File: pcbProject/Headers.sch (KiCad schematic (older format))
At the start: 4 parts, among them P1 Power Header, P2 Analog Header (AD), P3 Digital Header 02 (IOH), P4 Digital Header 01 (IOL)

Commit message: schema Afgewerkt
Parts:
- removed P2: Analog Header (AD), ~, symbol Arduino_Uno_R3_From_Scratch-rescue:CONN_01X06
- added P2: P2 Analog Header (AD), symbol Arduino_Uno_R3_From_Scratch-rescue:CONN_01X08
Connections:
- net ARD_AN0: now also P2.1 (P1)
- net ARD_AN1: now also P2.2 (P2)
- net ARD_AN2: now also P2.3 (P3)
- net ARD_AN3: now also P2.4 (P4)
- net ARD_AN4/SDA: now also P2.5 (P5)
- net ARD_AN5/SCL: now also P2.6 (P6)
- new net ARD_AN6: P2.7 (P7)
- new net ARD_AN7: P2.8 (P8)
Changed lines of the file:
@@
 $EndDescr
-$Comp
-L Arduino_Uno_R3_From_Scratch-rescue:CONN_01X06 P2
-U 1 1 55E94764
-P 6250 3325
-F 0 "P2" H 6400 3200 60  0000 L CNN
-F 1 "Analog Header (AD)" H 6400 3325 60  0000 L CNN
-F 2 "~" H 6250 3325 60  0000 C CNN
-F 3 "http://sullinscorp.com/catalogs/101_PAGE114-115_.100_FEMALE_HDR.pdf" H 6250 3325 60  0001 C CNN
-F 4 "Connector Header 6 Position 0.100\" (2.54mm) Gold Surface Mount" H 6250 3325 60  0001 C CNN "Characteristics"
-F 5 "Shield Header 6POS - ANLG" H 6250 3325 60  0001 C CNN "Description"
-F 6 "Sullins Connector" H 6250 3325 60  0001 C CNN "MFN"
-F 7 "NPPC061KFXC-RC" H 6250 3325 60  0001 C CNN "MFP"
-F 8 "SMD" H 6250 3325 60  0001 C CNN "Package ID"
-F 9 "ANY" H 6250 3325 60  0001 C CNN "Source"
-F 10 "N" H 6250 3325 60  0001 C CNN "Critical"
-F 11 "Shield_Headers" H 6250 3325 60  0001 C CNN "Subsystem"
-F 12 "~" H 6250 3325 60  0001 C CNN "Notes"
-	1    6250 3325
-	1    0    0    1
-$EndComp
 $Comp
 L Arduino_Uno_R3_From_Scratch:5V_LDO #PWR035
@@
 Text HLabel 4800 2725 0    40   Input ~ 0
 328P_RESET
-Text HLabel 4775 3275 0    40   Input ~ 0
+Text HLabel 4800 3475 0    40   Input ~ 0
 ARD_AN3
-Text HLabel 4775 3375 0    40   Input ~ 0
+Text HLabel 4800 3575 0    40   Input ~ 0
 ARD_AN2
-Text HLabel 4775 3475 0    40   Input ~ 0
+Text HLabel 4800 3675 0    40   Input ~ 0
 ARD_AN1
-Text HLabel 4775 3575 0    40   Input ~ 0
+Text HLabel 4800 3775 0    40   Input ~ 0
 ARD_AN0
-Wire Wire Line
-	4775 3575 6050 3575
-Wire Wire Line
-	6050 3475 4775 3475
-Wire Wire Line
-	4775 3375 6050 3375
-Wire Wire Line
-	6050 3275 4775 3275
 Text HLabel 4775 5175 0    40   Input ~ 0
 ARD_DIG7
@@
 	1    0    0    -1
 $EndComp
-Text HLabel 4800 3175 0    40   Input ~ 0
+Text HLabel 4825 3375 0    40   Input ~ 0
 ARD_AN4/SDA
-Text HLabel 4800 3075 0    40   Input ~ 0
+Text HLabel 4825 3275 0    40   Input ~ 0
 ARD_AN5/SCL
-Wire Wire Line
-	4800 3075 6050 3075
-Wire Wire Line
-	4800 3175 6050 3175
 Text HLabel 4750 4800 0    40   Input ~ 0
 ARD_DIG8
@@
 Wire Wire Line
 	6050 4700 4750 4700
+$Comp
+L Arduino_Uno_R3_From_Scratch-rescue:CONN_01X08 P2
+U 1 1 5C79CCDA
+P 6250 3425
+F 0 "P2" H 6168 2850 50  0000 C CNN
+F 1 "P2 Analog Header (AD)" H 6825 3400 50  0000 C CNN
+F 2 "" H 6250 3425 60  0000 C CNN
+F 3 "" H 6250 3425 60  0000 C CNN
+	1    6250 3425
+	1    0    0    1
+$EndComp
+Wire Wire Line
+	4800 3775 6050 3775
+Wire Wire Line
+	4800 3675 6050 3675
+Wire Wire Line
+	4800 3575 6050 3575
+Wire Wire Line
+	4800 3475 6050 3475
+Wire Wire Line
+	4825 3375 6050 3375
+Wire Wire Line
+	4825 3275 6050 3275
+Text HLabel 4825 3175 0    50   Input ~ 0
+ARD_AN6
+Text HLabel 4825 3075 0    50   Input ~ 0
+ARD_AN7
+Wire Wire Line
+	4825 3175 6050 3175
+Wire Wire Line
+	4825 3075 6050 3075
 $EndSCHEMATC

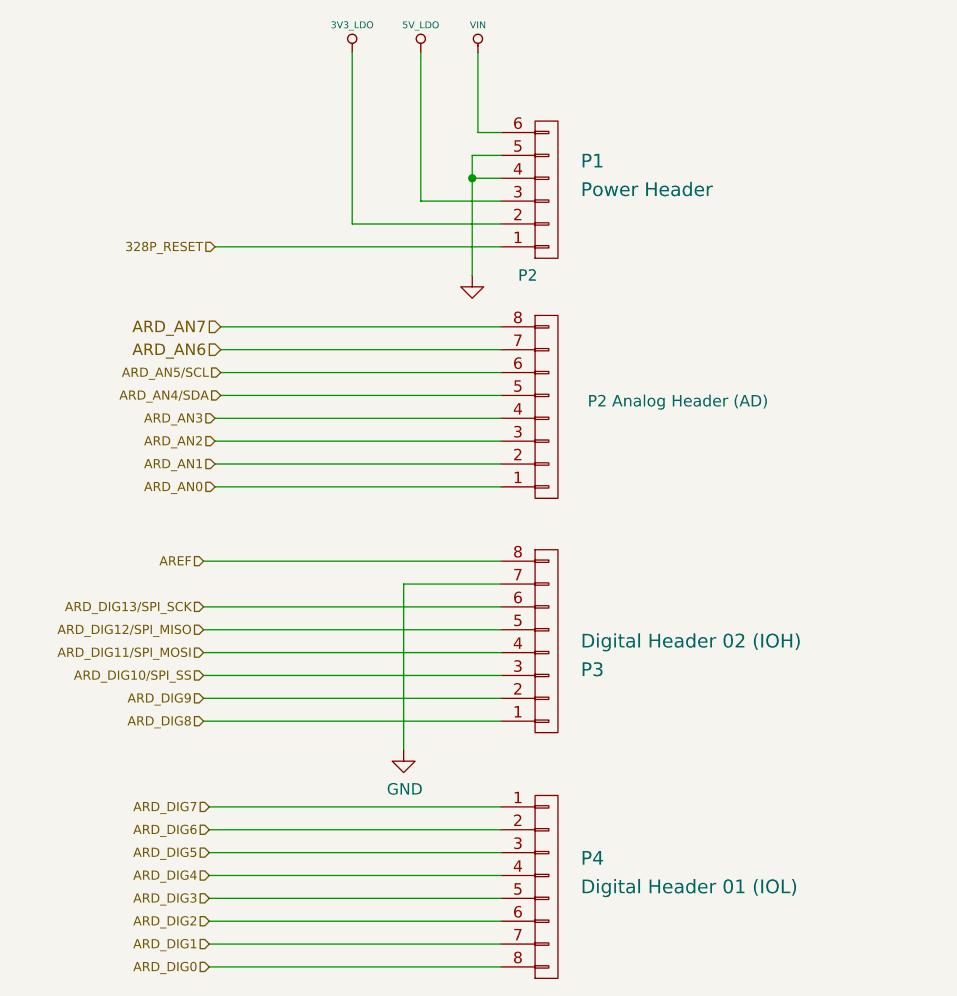
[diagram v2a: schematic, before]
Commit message: TekeningAfenGecontroleerd
nu nog componenten toevoegen en routen
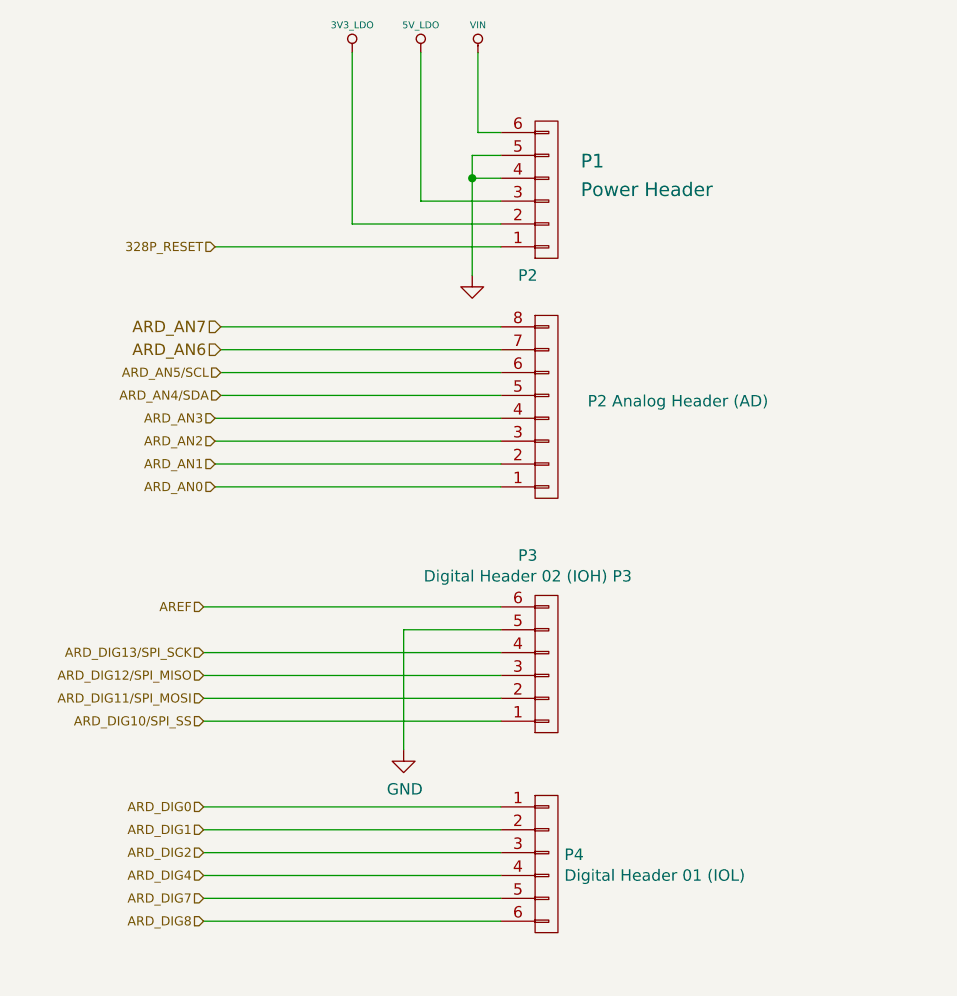
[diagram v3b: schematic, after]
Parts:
- removed P3: Digital Header 02 (IOH), ~, symbol Arduino_Uno_R3_From_Scratch-rescue:CONN_01X08
- removed P4: Digital Header 01 (IOL), ~, symbol Arduino_Uno_R3_From_Scratch-rescue:CONN_01X08
- added P3: Digital Header 02 (IOH) P3, symbol Arduino_Uno_R3_From_Scratch-rescue:CONN_01X06
- added P4: Digital Header 01 (IOL), symbol Arduino_Uno_R3_From_Scratch-rescue:CONN_01X06
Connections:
- net ARD_DIG0: now also P4.1 (P1)
- net ARD_DIG1: now also P4.2 (P2)
- net ARD_DIG10/SPI_SS: now also P3.1 (P1)
- net ARD_DIG11/SPI_MOSI: now also P3.2 (P2)
- net ARD_DIG12/SPI_MISO: now also P3.3 (P3)
- net ARD_DIG13/SPI_SCK: now also P3.4 (P4)
- net ARD_DIG2: now also P4.3 (P3)
- net ARD_DIG4: now also P4.4 (P4)
- net ARD_DIG7: now also P4.5 (P5)
- net ARD_DIG8: now also P4.6 (P6)
- net AREF: now also P3.6 (P6)
- net GND: now also P3.5 (P5)
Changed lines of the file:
@@
 Text HLabel 4800 3775 0    40   Input ~ 0
 ARD_AN0
-Text HLabel 4775 5175 0    40   Input ~ 0
+Text HLabel 4750 5575 0    40   Input ~ 0
 ARD_DIG7
-Text HLabel 4775 5275 0    40   Input ~ 0
-ARD_DIG6
-Text HLabel 4775 5375 0    40   Input ~ 0
-ARD_DIG5
-Text HLabel 4775 5475 0    40   Input ~ 0
+Text HLabel 4750 5475 0    40   Input ~ 0
 ARD_DIG4
-Text HLabel 4775 5575 0    40   Input ~ 0
-ARD_DIG3
-Text HLabel 4775 5675 0    40   Input ~ 0
+Text HLabel 4750 5375 0    40   Input ~ 0
 ARD_DIG2
-Text HLabel 4775 5775 0    40   Input ~ 0
+Text HLabel 4750 5275 0    40   Input ~ 0
 ARD_DIG1
-Text HLabel 4775 5875 0    40   Input ~ 0
+Text HLabel 4750 5175 0    40   Input ~ 0
 ARD_DIG0
-Wire Wire Line
-	6050 5175 4775 5175
-Wire Wire Line
-	4775 5275 6050 5275
-Wire Wire Line
-	6050 5375 4775 5375
-Wire Wire Line
-	4775 5475 6050 5475
-Wire Wire Line
-	6050 5575 4775 5575
-Wire Wire Line
-	4775 5675 6050 5675
-Wire Wire Line
-	6050 5775 4775 5775
-Wire Wire Line
-	4775 5875 6050 5875
-$Comp
-L Arduino_Uno_R3_From_Scratch-rescue:CONN_01X08 P4
-U 1 1 5615BF57
-P 6250 5525
-F 0 "P4" H 6400 5650 60  0000 L CNN
-F 1 "Digital Header 01 (IOL)" H 6400 5525 60  0000 L CNN
-F 2 "~" H 6250 5525 60  0000 C CNN
-F 3 "http://sullinscorp.com/catalogs/101_PAGE114-115_.100_FEMALE_HDR.pdf" H 6250 5525 60  0001 C CNN
-F 4 "Connector Header 8 Position 0.100\" (2.54mm) Gold Surface Mount" H 6250 5525 60  0001 C CNN "Characteristics"
-F 5 "Shield Header 8POS - DIG01" H 6250 5525 60  0001 C CNN "Description"
-F 6 "Sullins Connector" H 6250 5525 60  0001 C CNN "MFN"
-F 7 "NPPC081KFXC-RC" H 6250 5525 60  0001 C CNN "MFP"
-F 8 "SMD" H 6250 5525 60  0001 C CNN "Package ID"
-F 9 "ANY" H 6250 5525 60  0001 C CNN "Source"
-F 10 "N" H 6250 5525 60  0001 C CNN "Critical"
-F 11 "Shield_Headers" H 6250 5525 60  0001 C CNN "Subsystem"
-F 12 "~" H 6250 5525 60  0001 C CNN "Notes"
-	1    6250 5525
-	1    0    0    -1
-$EndComp
 Text HLabel 4825 3375 0    40   Input ~ 0
 ARD_AN4/SDA
 Text HLabel 4825 3275 0    40   Input ~ 0
 ARD_AN5/SCL
+Text HLabel 4750 5675 0    40   Input ~ 0
+ARD_DIG8
 Text HLabel 4750 4800 0    40   Input ~ 0
-ARD_DIG8
+ARD_DIG10/SPI_SS
 Text HLabel 4750 4700 0    40   Input ~ 0
-ARD_DIG9
+ARD_DIG11/SPI_MOSI
 Text HLabel 4750 4600 0    40   Input ~ 0
-ARD_DIG10/SPI_SS
+ARD_DIG12/SPI_MISO
 Text HLabel 4750 4500 0    40   Input ~ 0
-ARD_DIG11/SPI_MOSI
-Text HLabel 4750 4400 0    40   Input ~ 0
-ARD_DIG12/SPI_MISO
+ARD_DIG13/SPI_SCK
 Text HLabel 4750 4300 0    40   Input ~ 0
-ARD_DIG13/SPI_SCK
-Text HLabel 4750 4100 0    40   Input ~ 0
 AREF
 $Comp
@@
 	5950 2225 6050 2225
 $Comp
-L Arduino_Uno_R3_From_Scratch-rescue:CONN_01X08 P3
-U 1 1 5C578D54
-P 6250 4450
-F 0 "P3" H 6400 4575 60  0000 L CNN
-F 1 "Digital Header 02 (IOH)" H 6400 4450 60  0000 L CNN
-F 2 "~" H 6250 4450 60  0000 C CNN
-F 3 "http://sullinscorp.com/catalogs/101_PAGE114-115_.100_FEMALE_HDR.pdf" H 6250 4450 60  0001 C CNN
-F 4 "Connector Header 8 Position 0.100\" (2.54mm) Gold Surface Mount" H 6250 4450 60  0001 C CNN "Characteristics"
-F 5 "Shield Header 8POS - DIG01" H 6250 4450 60  0001 C CNN "Description"
-F 6 "Sullins Connector" H 6250 4450 60  0001 C CNN "MFN"
-F 7 "NPPC081KFXC-RC" H 6250 4450 60  0001 C CNN "MFP"
-F 8 "SMD" H 6250 4450 60  0001 C CNN "Package ID"
-F 9 "ANY" H 6250 4450 60  0001 C CNN "Source"
-F 10 "N" H 6250 4450 60  0001 C CNN "Critical"
-F 11 "Shield_Headers" H 6250 4450 60  0001 C CNN "Subsystem"
-F 12 "~" H 6250 4450 60  0001 C CNN "Notes"
-	1    6250 4450
-	1    0    0    1
-$EndComp
-Wire Wire Line
-	6050 4100 4750 4100
-$Comp
 L power:GND #PWR0101
 U 1 1 5C579B64
@@
 $EndComp
 Wire Wire Line
-	6050 4200 5625 4200
-Wire Wire Line
-	5625 4200 5625 4925
-Wire Wire Line
 	6050 4300 4750 4300
-Wire Wire Line
-	6050 4400 4750 4400
 Wire Wire Line
 	6050 4500 4750 4500
 Wire Wire Line
 	6050 4600 4750 4600
-Wire Wire Line
-	6050 4800 4750 4800
-Wire Wire Line
-	6050 4700 4750 4700
 $Comp
 L Arduino_Uno_R3_From_Scratch-rescue:CONN_01X08 P2
@@
 Wire Wire Line
 	4825 3075 6050 3075
+Wire Wire Line
+	4750 5175 6050 5175
+Wire Wire Line
+	4750 5275 6050 5275
+Wire Wire Line
+	4750 5375 6050 5375
+Wire Wire Line
+	4750 5475 6050 5475
+Wire Wire Line
+	4750 5575 6050 5575
+Wire Wire Line
+	4750 5675 6050 5675
+Wire Wire Line
+	4750 4800 6050 4800
+Wire Wire Line
+	4750 4700 6050 4700
+Wire Wire Line
+	6050 4400 5625 4400
+Wire Wire Line
+	5625 4400 5625 4925
+$Comp
+L Arduino_Uno_R3_From_Scratch-rescue:CONN_01X06 P3
+U 1 1 5C9A72A7
+P 6250 4550
+F 0 "P3" H 6168 4075 50  0000 C CNN
+F 1 "Digital Header 02 (IOH) P3" H 6168 4166 50  0000 C CNN
+F 2 "" H 6250 4550 60  0000 C CNN
+F 3 "" H 6250 4550 60  0000 C CNN
+	1    6250 4550
+	1    0    0    1
+$EndComp
+$Comp
+L Arduino_Uno_R3_From_Scratch-rescue:CONN_01X06 P4
+U 1 1 5C9A74BA
+P 6250 5425
+F 0 "P4" H 6328 5466 50  0000 L CNN
+F 1 "Digital Header 01 (IOL)" H 6328 5375 50  0000 L CNN
+F 2 "" H 6250 5425 60  0000 C CNN
+F 3 "" H 6250 5425 60  0000 C CNN
+	1    6250 5425
+	1    0    0    -1
+$EndComp
 $EndSCHEMATC

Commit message: deel1routingpcb
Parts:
- P1: footprint ~ -> Connector_PinSocket_2.54mm:PinSocket_1x06_P2.54mm_Vertical
- P2: footprint (none) -> Connector_PinSocket_2.54mm:PinSocket_1x08_P2.54mm_Vertical
- P3, P4: footprint (none) -> Connector_PinSocket_2.54mm:PinSocket_1x06_P2.54mm_Vertical
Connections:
- net Vin is gone; now on net 3V3_LDO: P1.6 (P6)
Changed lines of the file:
@@
-	1    0    0    -1
-$EndComp
-$Comp
-L Arduino_Uno_R3_From_Scratch:Vin #PWR037
-U 1 1 55E95DA2
-P 5950 1875
-F 0 "#PWR037" H 5950 1965 20  0001 C CNN
-F 1 "VIN" H 5950 1995 30  0000 C CNN
-F 2 "~" H 5950 1875 60  0000 C CNN
-F 3 "~" H 5950 1875 60  0000 C CNN
-	1    5950 1875
 	1    0    0    -1
 $EndComp
@@
 F 0 "P1" H 6400 2350 60  0000 L CNN
 F 1 "Power Header" H 6400 2475 60  0000 L CNN
-F 2 "~" H 6250 2475 60  0000 C CNN
+F 2 "Connector_PinSocket_2.54mm:PinSocket_1x06_P2.54mm_Vertical" H 6250 2475 60  0000 C CNN
 F 3 "http://sullinscorp.com/catalogs/101_PAGE114-115_.100_FEMALE_HDR.pdf" H 6250 2475 60  0001 C CNN
 F 4 "Connector Header 6 Position 0.100\" (2.54mm) Gold Surface Mount" H 6250 2475 60  0001 C CNN "Characteristics"
@@
 	5400 2625 6050 2625
 Wire Wire Line
-	5400 1875 5400 2625
+	5400 1875 5400 2225
 Wire Wire Line
 	5700 2525 6050 2525
@@
 Wire Wire Line
 	5925 2425 5925 2850
-Wire Wire Line
-	5950 1875 5950 2225
-Wire Wire Line
-	5950 2225 6050 2225
 $Comp
 L power:GND #PWR0101
@@
 F 0 "P2" H 6168 2850 50  0000 C CNN
 F 1 "P2 Analog Header (AD)" H 6825 3400 50  0000 C CNN
-F 2 "" H 6250 3425 60  0001 C CNN
+F 2 "Connector_PinSocket_2.54mm:PinSocket_1x08_P2.54mm_Vertical" H 6250 3425 60  0001 C CNN
 F 3 "" H 6250 3425 60  0000 C CNN
 	1    6250 3425
@@
 F 0 "P3" H 6168 4075 50  0000 C CNN
 F 1 "Digital Header 02 (IOH) P3" H 6168 4166 50  0000 C CNN
-F 2 "" H 6250 4550 60  0000 C CNN
+F 2 "Connector_PinSocket_2.54mm:PinSocket_1x06_P2.54mm_Vertical" H 6250 4550 60  0001 C CNN
 F 3 "" H 6250 4550 60  0000 C CNN
 	1    6250 4550
@@
 F 0 "P4" H 6328 5466 50  0000 L CNN
 F 1 "Digital Header 01 (IOL)" H 6328 5375 50  0000 L CNN
-F 2 "" H 6250 5425 60  0000 C CNN
+F 2 "Connector_PinSocket_2.54mm:PinSocket_1x06_P2.54mm_Vertical" H 6250 5425 60  0001 C CNN
 F 3 "" H 6250 5425 60  0000 C CNN
 	1    6250 5425
 	1    0    0    -1
 $EndComp
+Wire Wire Line
+	5400 2225 6050 2225
+Connection ~ 5400 2225
+Wire Wire Line
+	5400 2225 5400 2625
 $EndSCHEMATC

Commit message: pcb
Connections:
- net 328P_RESET: now also P1.6 (P6); no longer P1.1 (P1)
- net 3V3_LDO: now also P1.3 (P3), P1.4 (P4); no longer P1.2 (P2), P1.6 (P6)
- net 5V_LDO: now also P1.5 (P5); no longer P1.3 (P3)
- net GND: now also P1.1 (P1), P1.2 (P2); no longer P1.4 (P4), P1.5 (P5)
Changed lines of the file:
@@
 L Arduino_Uno_R3_From_Scratch:5V_LDO #PWR035
 U 1 1 55E95D7A
-P 5700 1875
-F 0 "#PWR035" H 5700 1965 20  0001 C CNN
-F 1 "5V_LDO" H 5700 1995 30  0000 C CNN
-F 2 "~" H 5700 1875 60  0000 C CNN
-F 3 "~" H 5700 1875 60  0000 C CNN
-	1    5700 1875
+P 5625 1875
+F 0 "#PWR035" H 5625 1965 20  0001 C CNN
+F 1 "5V_LDO" H 5625 1995 30  0000 C CNN
+F 2 "~" H 5625 1875 60  0000 C CNN
+F 3 "~" H 5625 1875 60  0000 C CNN
+	1    5625 1875
 	1    0    0    -1
 $EndComp
@@
 	1    0    0    -1
 $EndComp
-Text HLabel 4800 2725 0    40   Input ~ 0
+Text HLabel 5925 2225 0    40   Input ~ 0
 328P_RESET
 Text HLabel 4800 3475 0    40   Input ~ 0
@@
 	1    0    0    1
 $EndComp
-Wire Wire Line
-	4800 2725 6050 2725
 $Comp
 L power:GND #PWR038
@@
 	1    0    0    -1
 $EndComp
-Wire Wire Line
-	5400 2625 6050 2625
-Wire Wire Line
-	5400 1875 5400 2225
-Wire Wire Line
-	5700 2525 6050 2525
-Wire Wire Line
-	5700 1875 5700 2525
-Wire Wire Line
-	6050 2325 5925 2325
-Wire Wire Line
-	6050 2425 5925 2425
-Wire Wire Line
-	5925 2325 5925 2425
-Connection ~ 5925 2425
-Wire Wire Line
-	5925 2425 5925 2850
 $Comp
 L power:GND #PWR0101
@@
 $EndComp
 Wire Wire Line
-	5400 2225 6050 2225
-Connection ~ 5400 2225
-Wire Wire Line
-	5400 2225 5400 2625
+	5925 2225 6050 2225
+Wire Wire Line
+	5925 2850 5925 2725
+Wire Wire Line
+	5925 2725 6050 2725
+Wire Wire Line
+	5925 2725 5925 2625
+Wire Wire Line
+	5925 2625 6050 2625
+Connection ~ 5925 2725
+Wire Wire Line
+	6050 2525 5400 2525
+Wire Wire Line
+	5400 2425 6050 2425
+Wire Wire Line
+	5400 1875 5400 2425
+Connection ~ 5400 2425
+Wire Wire Line
+	5400 2425 5400 2525
+Wire Wire Line
+	5625 1875 5625 2325
+Wire Wire Line
+	5625 2325 6050 2325
 $EndSCHEMATC
